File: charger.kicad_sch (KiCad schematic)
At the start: 14 parts, among them U2 LTC4121IUDTRPBF

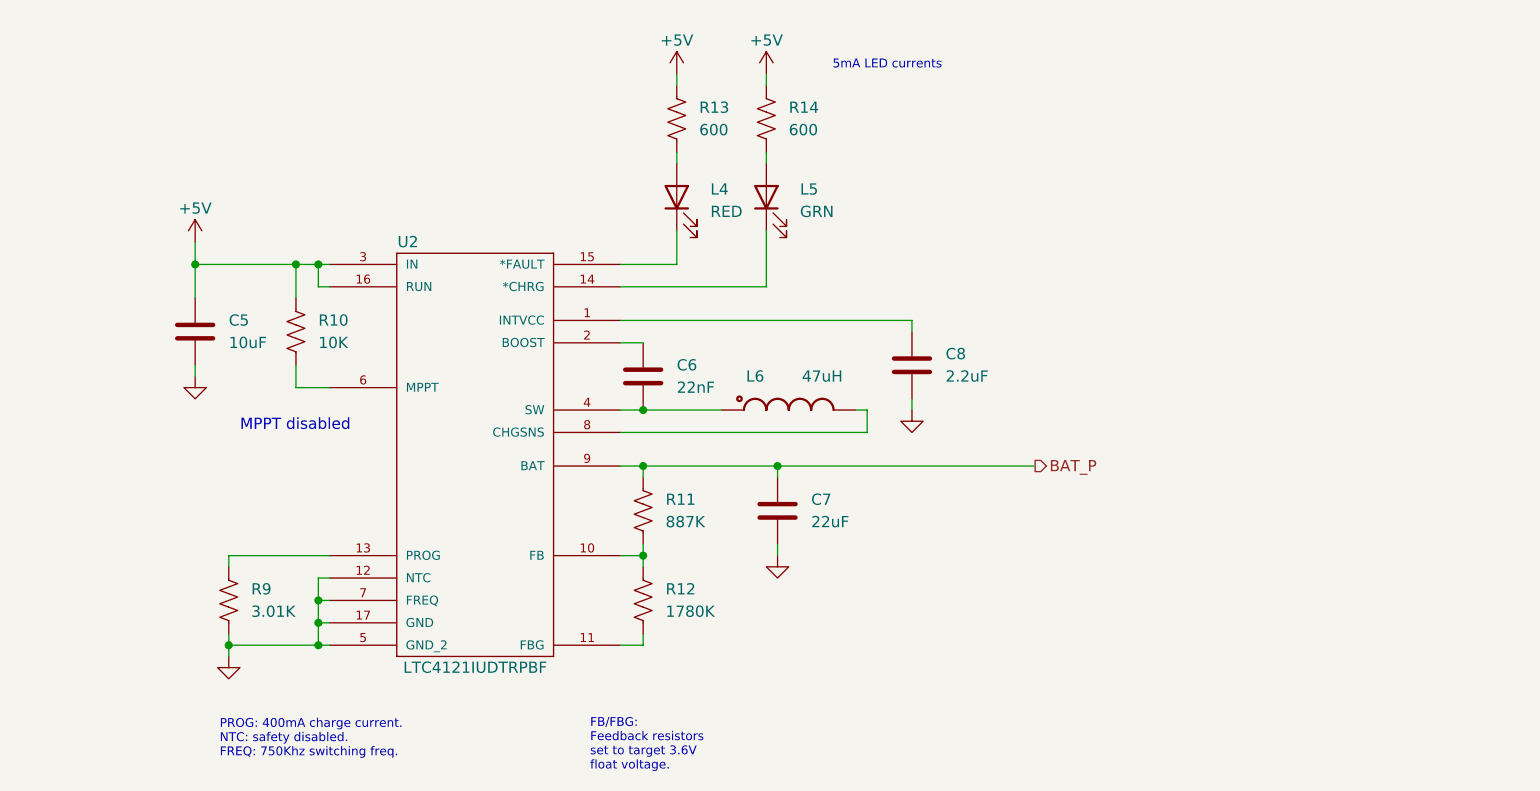
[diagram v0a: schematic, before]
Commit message: [WIP] Schematic updated with reverse blocking FETs
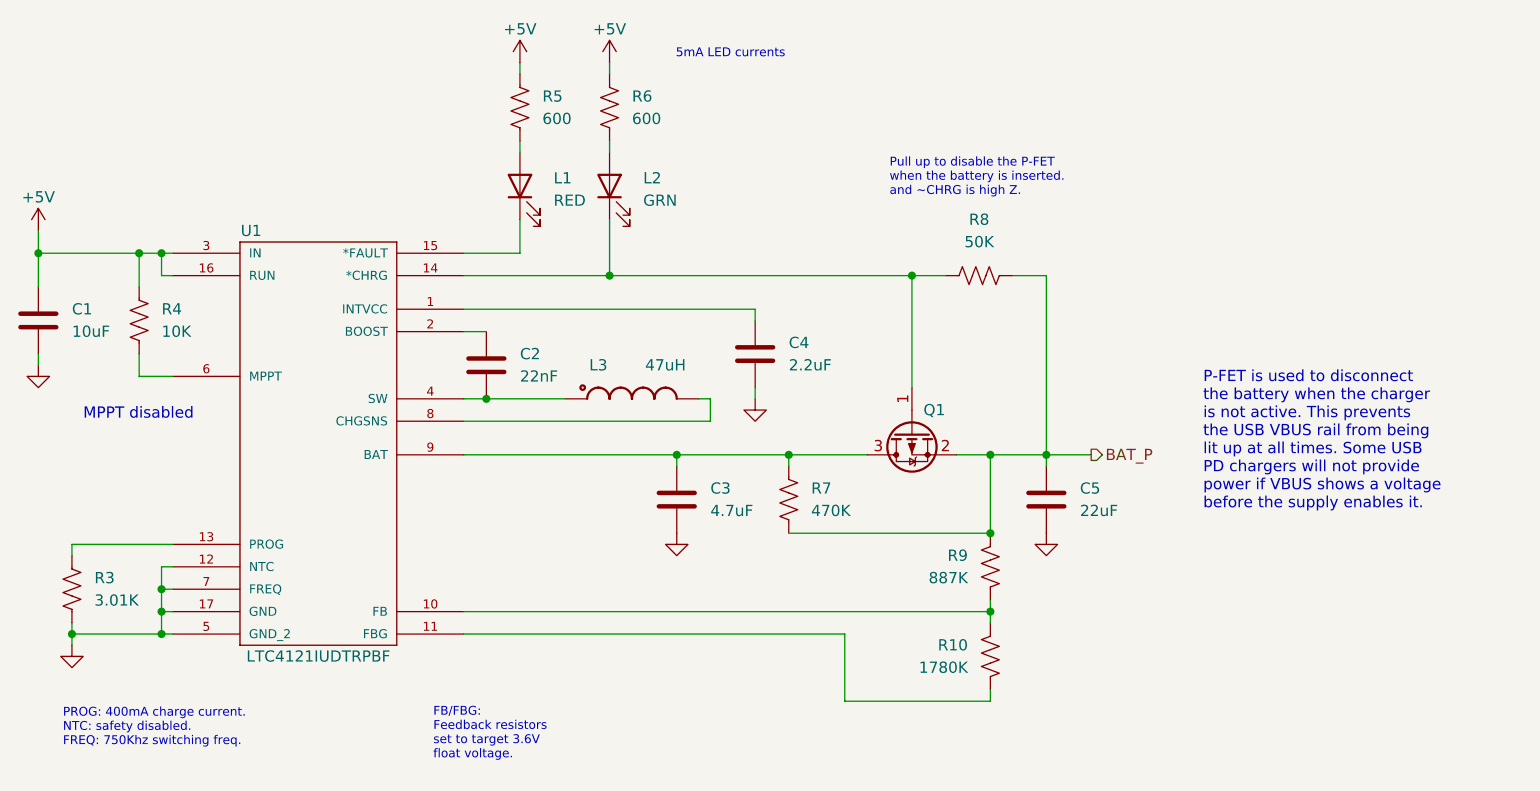
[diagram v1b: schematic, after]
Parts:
- added C3: 4.7uF, Capacitor_SMD:C_0402_1005Metric, symbol Device:C
- added Q1: SI2343DS, Package_TO_SOT_SMD:SOT-23, symbol Transistor_FET:IRLML5203
- added R7: 470K, Resistor_SMD:R_0402_1005Metric, symbol Device:R_US
- added R8: 50K, Resistor_SMD:R_0402_1005Metric, symbol Device:R_US
- renumbered C5 to C1, C6 to C2, C8 to C4, C7 to C5, L4 to L1, L5 to L2, L6 to L3, R12 to R10, R9 to R3, R10 to R4, R13 to R5, R14 to R6, R11 to R9, U2 to U1
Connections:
- net BAT_P: now also Q1.2 (S), R7.2, R8.2; no longer U1.9 (BAT)
- net GND: now also C3.2
- net at L2.1 (K), U1.14 (*CHRG): now also Q1.1 (G), R8.1
- new net: C3.1, Q1.3 (D), R7.1, U1.9 (BAT)
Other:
- note added: "P-FET is used to disconnect the battery when the charger is not active. This prevents the USB VBUS rail from being lit up at all times. Some USB PD chargers will not provide power if VBUS shows a voltage before the supply enables it."
- note added: "Pull up to disable the P-FET when the battery is inserted. and ~CHRG is high Z."
- moved on the sheet: C1, C2, C4, C5, L1, L2, L3, R10, R3, R4, R5, R6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
